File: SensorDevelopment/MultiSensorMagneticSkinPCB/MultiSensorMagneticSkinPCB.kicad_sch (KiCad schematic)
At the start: 13 parts, among them J2 Conn_01x05, U2 DRV5056A4EDBZRQ1, U3 DRV5056A4EDBZRQ1, U4 DRV5056A4EDBZRQ1

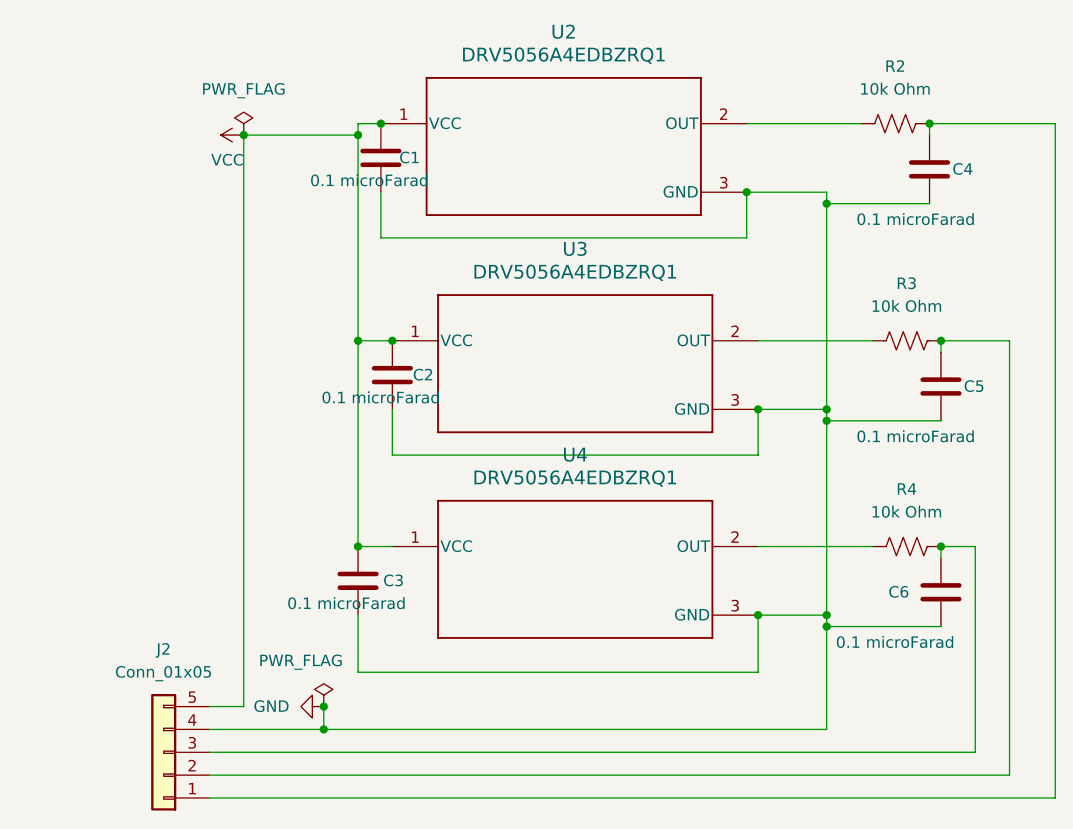
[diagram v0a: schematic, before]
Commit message: Updated sensor data script to detect touches. Did PCB Layout for a multisensor board
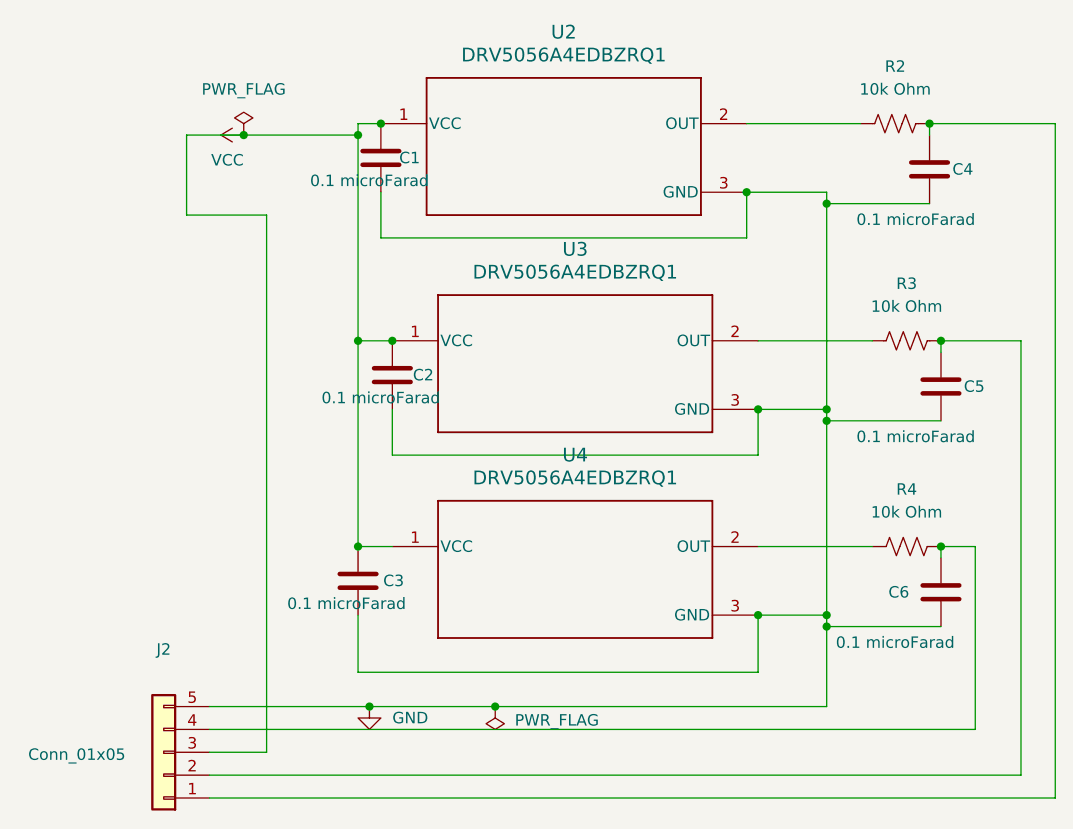
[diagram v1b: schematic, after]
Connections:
- net GND: now also J2.5 (Pin_5); no longer J2.4 (Pin_4)
- net VCC: now also J2.3 (Pin_3); no longer J2.5 (Pin_5)
- net at C6.1, R4.2: now also J2.4 (Pin_4); no longer J2.3 (Pin_3)
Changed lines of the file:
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@@
+	)
+	(junction
+		(at 113.03 110.49)
+		(diameter 0)
+		(color 0 0 0 0)
 	)
 	(junction
@@
 	)
 	(junction
-		(at 107.95 110.49)
-		(diameter 0)
-		(color 0 0 0 0)
-	)
-	(junction
 		(at 111.76 69.85)
 		(diameter 0)
@@
 	)
 	(junction
-		(at 107.95 113.03)
-		(diameter 0)
-		(color 0 0 0 0)
-	)
-	(junction
 		(at 163.83 100.33)
 		(diameter 0)
@@
 	)
 	(junction
+		(at 127 110.49)
+		(diameter 0)
+		(color 0 0 0 0)
+	)
+	(junction
 		(at 175.26 45.72)
 		(diameter 0)
@@
 	(wire
 		(pts
-			(xy 95.25 113.03) (xy 107.95 113.03)
-		)
-		(stroke
-			(width 0)
-			(type default)
-		)
-	)
-	(wire
-		(pts
 			(xy 163.83 54.61) (xy 163.83 53.34)
 		)
@@
 	(wire
 		(pts
-			(xy 184.15 69.85) (xy 184.15 118.11)
-		)
-		(stroke
-			(width 0)
-			(type default)
-		)
-	)
-	(wire
-		(pts
 			(xy 189.23 45.72) (xy 175.26 45.72)
 		)
@@
 	(wire
 		(pts
-			(xy 99.06 46.99) (xy 99.06 110.49)
-		)
-		(stroke
-			(width 0)
-			(type default)
-		)
-	)
-	(wire
-		(pts
 			(xy 156.21 106.68) (xy 156.21 100.33)
 		)
@@
 	(wire
 		(pts
+			(xy 101.6 115.57) (xy 95.25 115.57)
+		)
+		(stroke
+			(width 0)
+			(type default)
+		)
+	)
+	(wire
+		(pts
 			(xy 156.21 77.47) (xy 163.83 77.47)
 		)
@@
 	(wire
 		(pts
-			(xy 95.25 120.65) (xy 189.23 120.65)
+			(xy 189.23 45.72) (xy 189.23 120.65)
 		)
 		(stroke
@@
 	(wire
 		(pts
+			(xy 185.42 118.11) (xy 95.25 118.11)
+		)
+		(stroke
+			(width 0)
+			(type default)
+		)
+	)
+	(wire
+		(pts
 			(xy 156.21 69.85) (xy 168.91 69.85)
 		)
@@
 	(wire
 		(pts
-			(xy 99.06 110.49) (xy 95.25 110.49)
-		)
-		(stroke
-			(width 0)
-			(type default)
-		)
-	)
-	(wire
-		(pts
-			(xy 180.34 92.71) (xy 180.34 115.57)
-		)
-		(stroke
-			(width 0)
-			(type default)
-		)
-	)
-	(wire
-		(pts
 			(xy 156.21 92.71) (xy 168.91 92.71)
 		)
@@
 	(wire
 		(pts
+			(xy 163.83 110.49) (xy 163.83 101.6)
+		)
+		(stroke
+			(width 0)
+			(type default)
+		)
+	)
+	(wire
+		(pts
 			(xy 163.83 54.61) (xy 175.26 54.61)
 		)
@@
 	(wire
 		(pts
+			(xy 101.6 55.88) (xy 101.6 115.57)
+		)
+		(stroke
+			(width 0)
+			(type default)
+		)
+	)
+	(wire
+		(pts
+			(xy 95.25 110.49) (xy 113.03 110.49)
+		)
+		(stroke
+			(width 0)
+			(type default)
+		)
+	)
+	(wire
+		(pts
 			(xy 115.57 82.55) (xy 156.21 82.55)
 		)
@@
 	(wire
 		(pts
-			(xy 176.53 69.85) (xy 184.15 69.85)
+			(xy 95.25 113.03) (xy 180.34 113.03)
+		)
+		(stroke
+			(width 0)
+			(type default)
+		)
+	)
+	(wire
+		(pts
+			(xy 176.53 69.85) (xy 185.42 69.85)
 		)
 		(stroke
@@
 	(wire
 		(pts
+			(xy 113.03 110.49) (xy 127 110.49)
+		)
+		(stroke
+			(width 0)
+			(type default)
+		)
+	)
+	(wire
+		(pts
 			(xy 111.76 69.85) (xy 115.57 69.85)
 		)
@@
 	(wire
 		(pts
-			(xy 189.23 120.65) (xy 189.23 45.72)
+			(xy 92.71 55.88) (xy 92.71 46.99)
 		)
 		(stroke
@@
 	(wire
 		(pts
-			(xy 95.25 115.57) (xy 180.34 115.57)
-		)
-		(stroke
-			(width 0)
-			(type default)
-		)
-	)
-	(wire
-		(pts
-			(xy 107.95 113.03) (xy 163.83 113.03)
+			(xy 101.6 55.88) (xy 92.71 55.88)
+		)
+		(stroke
+			(width 0)
+			(type default)
+		)
+	)
+	(wire
+		(pts
+			(xy 92.71 46.99) (xy 99.06 46.99)
+		)
+		(stroke
+			(width 0)
+			(type default)
+		)
+	)
+	(wire
+		(pts
+			(xy 127 110.49) (xy 163.83 110.49)
+		)
+		(stroke
+			(width 0)
+			(type default)
+		)
+	)
+	(wire
+		(pts
+			(xy 185.42 69.85) (xy 185.42 118.11)
 		)
 		(stroke
@@
 	(wire
 		(pts
+			(xy 189.23 120.65) (xy 95.25 120.65)
+		)
+		(stroke
+			(width 0)
+			(type default)
+		)
+	)
+	(wire
+		(pts
 			(xy 175.26 45.72) (xy 175.26 46.99)
 		)
@@
 	(wire
 		(pts
-			(xy 107.95 110.49) (xy 107.95 113.03)
-		)
-		(stroke
-			(width 0)
-			(type default)
-		)
-	)
-	(wire
-		(pts
 			(xy 163.83 101.6) (xy 163.83 100.33)
 		)
@@
 	(wire
 		(pts
-			(xy 184.15 118.11) (xy 95.25 118.11)
+			(xy 180.34 92.71) (xy 180.34 113.03)
 		)
 		(stroke
@@
 		(pts
 			(xy 111.76 92.71) (xy 115.57 92.71)
-		)
-		(stroke
-			(width 0)
-			(type default)
-		)
-	)
-	(wire
-		(pts
-			(xy 163.83 113.03) (xy 163.83 101.6)
 		)
 		(stroke
@@
 	(symbol
 		(lib_id "power:PWR_FLAG")
-		(at 107.95 110.49 0)
+		(at 127 110.49 180)
 		(unit 1)
 		(body_style 1)
@@
 		(dnp no)
 		(property "Reference" "#FLG04"
-			(at 107.95 108.585 0)
+			(at 127 112.395 0)
 			(hide yes)
 			(show_name no)
@@
 		)
 		(property "Value" "PWR_FLAG"
-			(at 105.41 105.41 0)
+			(at 133.858 112.014 0)
 			(show_name no)
 			(do_not_autoplace no)
@@
 		)
 		(property "Footprint" ""
-			(at 107.95 110.49 0)
+			(at 127 110.49 0)
 			(hide yes)
 			(show_name no)
@@
 		)
 		(property "Datasheet" ""
-			(at 107.95 110.49 0)
+			(at 127 110.49 0)
 			(hide yes)
 			(show_name no)
@@
 		)
 		(property "Description" "Special symbol for telling ERC where power comes from"
-			(at 107.95 110.49 0)
+			(at 127 110.49 0)
 			(hide yes)
 			(show_name no)
@@
 	(symbol
 		(lib_id "power:GND")
-		(at 107.95 110.49 270)
+		(at 113.03 110.49 0)
 		(unit 1)
 		(body_style 1)
@@
 		(fields_autoplaced yes)
 		(property "Reference" "#PWR04"
-			(at 101.6 110.49 0)
+			(at 113.03 116.84 0)
 			(hide yes)
 			(show_name no)
@@
 		)
 		(property "Value" "GND"
-			(at 104.14 110.4899 90)
-			(show_name no)
-			(do_not_autoplace no)
-			(effects
-				(font
-					(size 1.27 1.27)
-				)
-				(justify right)
+			(at 115.57 111.7599 0)
+			(show_name no)
+			(do_not_autoplace no)
+			(effects
+				(font
+					(size 1.27 1.27)
+				)
+				(justify left)
 			)
 		)
 		(property "Footprint" ""
-			(at 107.95 110.49 0)
+			(at 113.03 110.49 0)
 			(hide yes)
 			(show_name no)
@@
 		)
 		(property "Datasheet" ""
-			(at 107.95 110.49 0)
+			(at 113.03 110.49 0)
 			(hide yes)
 			(show_name no)
@@
 		)
 		(property "Description" "Power symbol creates a global label with name \"GND\" , ground"
-			(at 107.95 110.49 0)
+			(at 113.03 110.49 0)
 			(hide yes)
 			(show_name no)
@@
 		(in_pos_files yes)
 		(dnp no)
-		(fields_autoplaced yes)
 		(property "Reference" "J2"
 			(at 90.17 104.14 0)
@@
 		)
 		(property "Value" "Conn_01x05"
-			(at 90.17 106.68 0)
-			(show_name no)
-			(do_not_autoplace no)
+			(at 80.518 115.824 0)
+			(show_name no)
+			(do_not_autoplace no)
